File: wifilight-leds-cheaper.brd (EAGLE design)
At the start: 50.8 x 50.8 mm, 46 parts, among them Q1 BUK98180-100A, Q2 BUK98180-100A, Q3 BUK98180-100A, Q4 BUK98180-100A, U2 PCA9685

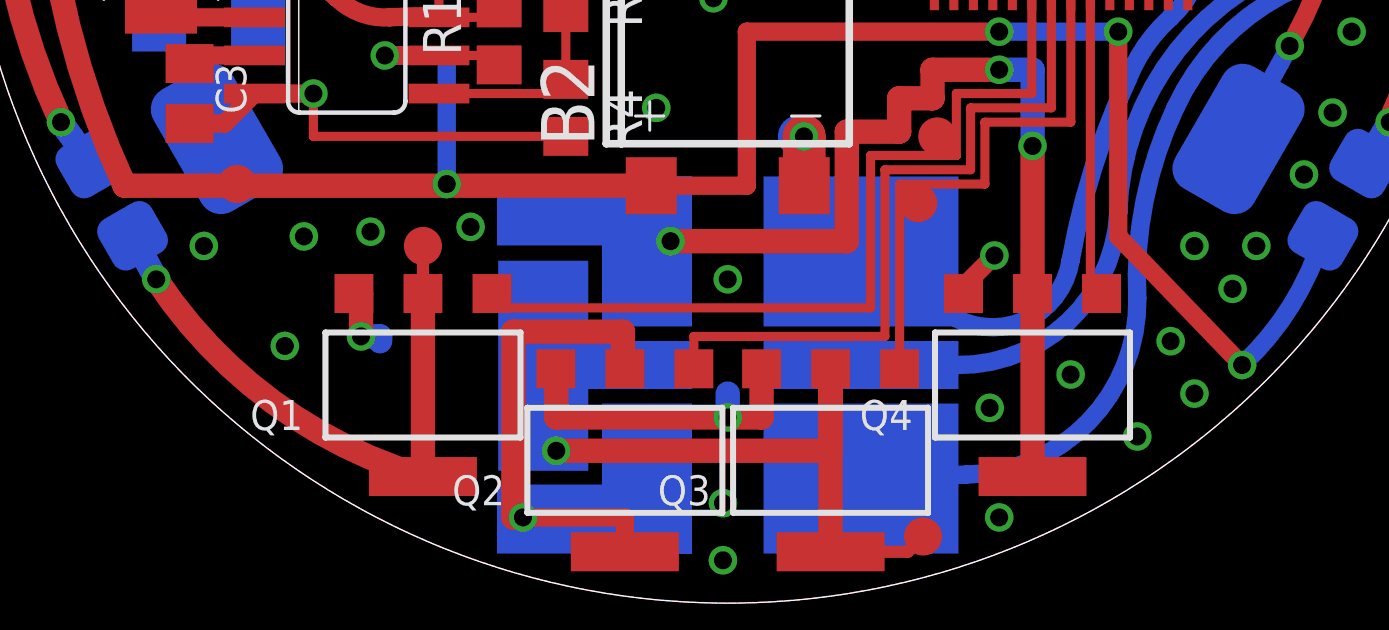
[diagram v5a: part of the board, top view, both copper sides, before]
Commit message: Add ground probe tag, drill locating hole in board.
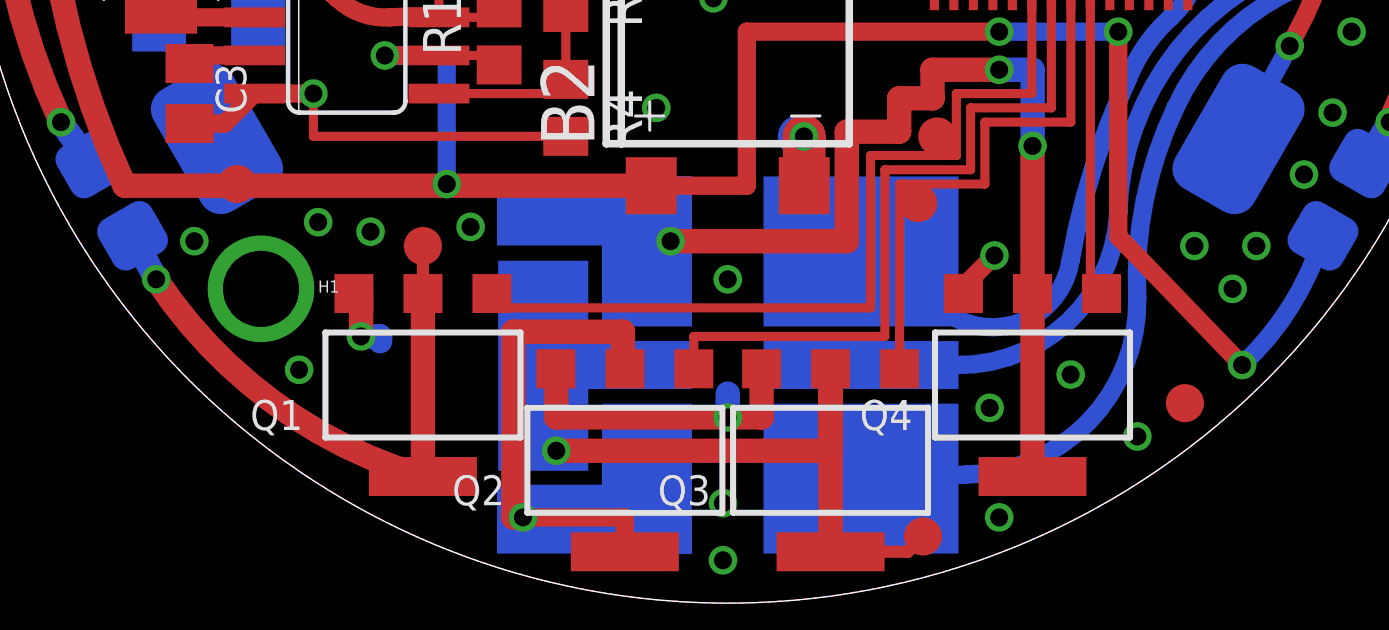
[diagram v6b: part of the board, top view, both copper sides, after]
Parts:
- added H1: SEW_HOLE, LilyPad-Wearables:SIMPLE_HOLE
- added TPGND: TEST-POINT3X5, SparkFun-Passives:PAD.03X.05
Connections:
- net GND: now also H1.P$1, TPGND.P$1
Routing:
- net GND: vias 75 -> 73
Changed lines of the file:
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@@
 <element name="P_WHITE" library="SparkFun-Passives" package="PAD.03X.05" value="TEST-POINT3X5" x="15.24" y="11.90625"/>
 <element name="P_RED" library="SparkFun-Passives" package="PAD.03X.05" value="TEST-POINT3X5" x="31.90875" y="2.2225"/>
+<element name="H1" library="LilyPad-Wearables" package="SIMPLE_HOLE" value="SEW_HOLE" x="9.8425" y="10.4775"/>
+<element name="TPGND" library="SparkFun-Passives" package="PAD.03X.05" value="TEST-POINT3X5" x="40.64" y="6.6675"/>
 </elements>
 <signals>
@@
 <via x="25.4" y="47.625" extent="1-16" drill="0.6"/>
 <via x="18.415" y="32.54375" extent="1-16" drill="0.6"/>
-<via x="7.9375" y="11.90625" extent="1-16" drill="0.6"/>
-<via x="11.27125" y="12.22375" extent="1-16" drill="0.6"/>
-<via x="10.63625" y="8.5725" extent="1-16" drill="0.6"/>
+<via x="7.62" y="12.065" extent="1-16" drill="0.6"/>
+<via x="11.7475" y="12.7" extent="1-16" drill="0.6"/>
+<via x="11.1125" y="7.77875" extent="1-16" drill="0.6"/>
 <via x="13.49375" y="12.3825" extent="1-16" drill="0.6"/>
 <via x="16.8275" y="12.54125" extent="1-16" drill="0.6"/>
@@
 <via x="34.44875" y="2.8575" extent="1-16" drill="0.6"/>
 <via x="39.0525" y="5.55625" extent="1-16" drill="0.6"/>
-<via x="40.9575" y="6.985" extent="1-16" drill="0.6"/>
-<via x="40.16375" y="8.73125" extent="1-16" drill="0.6"/>
 <via x="20.0025" y="26.19375" extent="1-16" drill="0.6"/>
 <via x="25.7175" y="26.82875" extent="1-16" drill="0.6"/>
@@
 <via x="24.92375" y="20.16125" extent="1-16" drill="0.6"/>
 <via x="23.01875" y="16.51" extent="1-16" drill="0.6"/>
+<contactref element="TPGND" pad="P$1"/>
+<contactref element="H1" pad="P$1"/>
 </signal>
 <signal name="SCL">

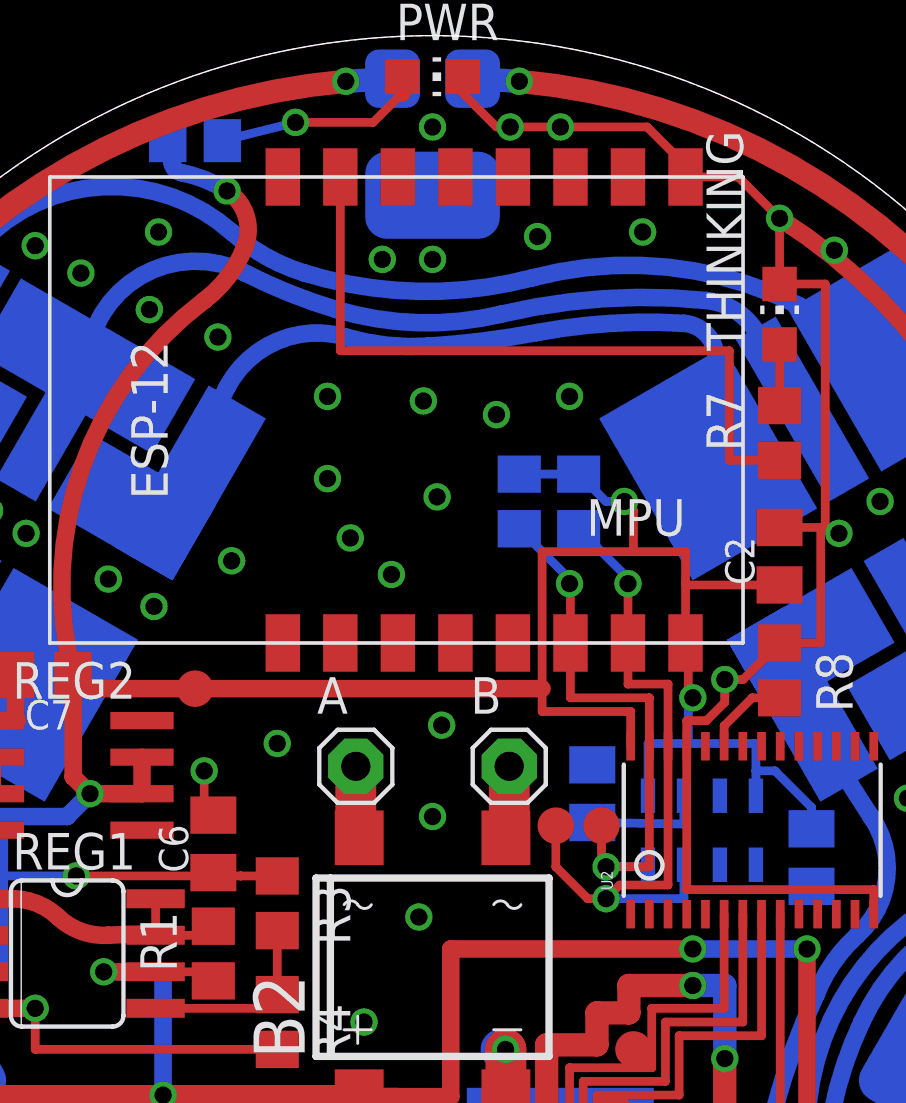
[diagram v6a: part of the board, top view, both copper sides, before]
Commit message: add SCL & SDA pins pogopins for programming
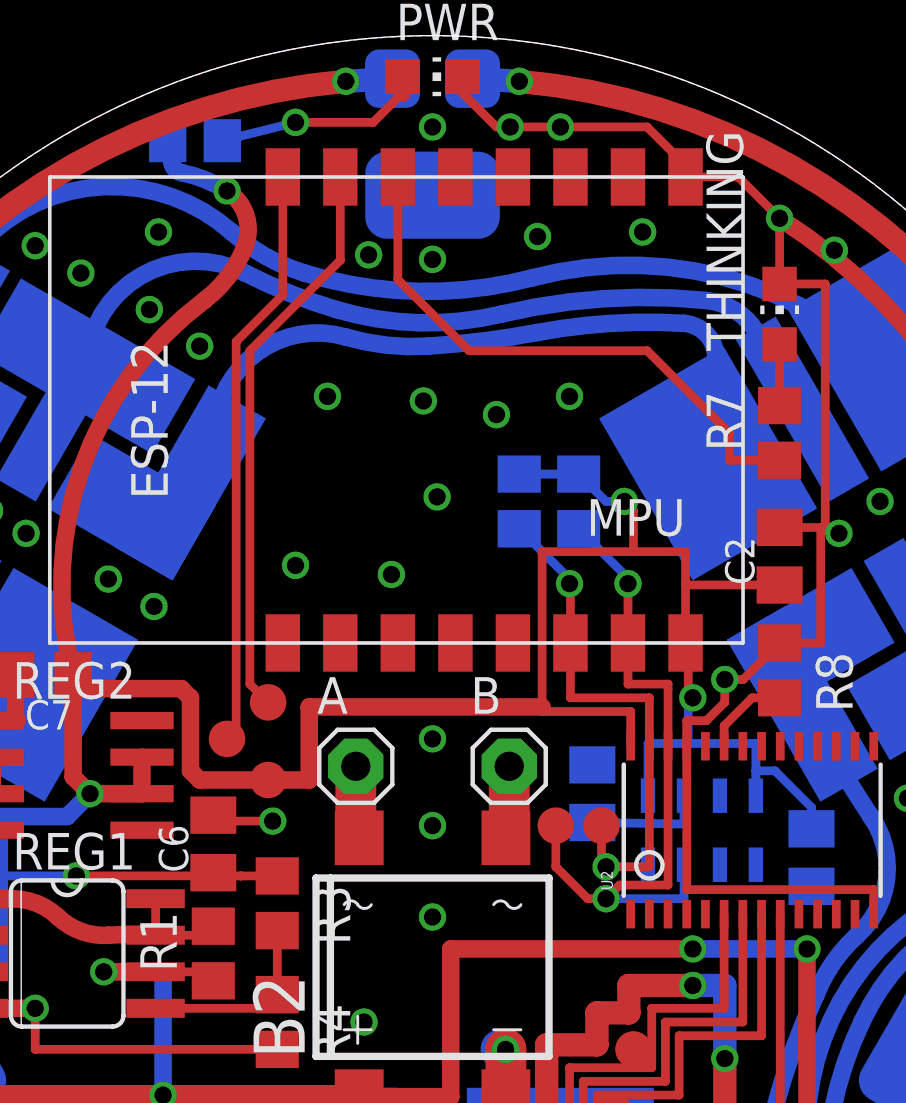
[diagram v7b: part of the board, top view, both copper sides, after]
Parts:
- added TPRX, TPTX: TEST-POINT3X5, SparkFun-Passives:PAD.03X.05
- moved TP3.3V 4.07 mm to (19.7, 24.9)
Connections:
- removed net N$29: MPU.9
- removed net N$32: MPU.6
- new net RXD: MPU.7, TPRX.P$1
- new net TXD: MPU.8, TPTX.P$1
- net RESET: now also MPU.9; no longer MPU.8
- net THINKING: now also MPU.6; no longer MPU.7
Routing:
- net TXD: track 0.00 -> 20.3 mm
- net RXD: track 0.00 -> 19.8 mm
- net 3.3V: track 96.0 -> 101.4 mm
- net THINKING: track 25.1 -> 20.0 mm
- net GND: track 128.2 -> 129.1 mm, vias 73 -> 70
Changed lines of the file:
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@@
 <element name="TP12V" library="SparkFun-Passives" package="PAD.03X.05" value="TEST-POINT3X5" x="9.04875" y="13.97"/>
 <element name="TP5V" library="SparkFun-Passives" package="PAD.03X.05" value="TEST-POINT3X5" x="4.7625" y="29.5275"/>
-<element name="TP3.3V" library="SparkFun-Passives" package="PAD.03X.05" value="TEST-POINT3X5" x="17.145" y="28.09875"/>
+<element name="TP3.3V" library="SparkFun-Passives" package="PAD.03X.05" value="TEST-POINT3X5" x="19.685" y="24.92375"/>
 <element name="SCL" library="SparkFun-Passives" package="PAD.03X.05" value="TEST-POINT3X5" x="29.68625" y="23.33625"/>
 <element name="SDA" library="SparkFun-Passives" package="PAD.03X.05" value="TEST-POINT3X5" x="31.27375" y="23.33625"/>
@@
 <element name="H1" library="LilyPad-Wearables" package="SIMPLE_HOLE" value="SEW_HOLE" x="9.8425" y="10.4775"/>
 <element name="TPGND" library="SparkFun-Passives" package="PAD.03X.05" value="TEST-POINT3X5" x="40.64" y="6.6675"/>
+<element name="TPTX" library="SparkFun-Passives" package="PAD.03X.05" value="TEST-POINT3X5" x="18.25625" y="26.3525"/>
+<element name="TPRX" library="SparkFun-Passives" package="PAD.03X.05" value="TEST-POINT3X5" x="19.685" y="27.6225"/>
 </elements>
 <signals>
@@
 <via x="6.35" y="26.51125" extent="1-16" drill="0.6"/>
 <wire x1="17.78" y1="23.70125" x2="17.4625" y2="23.70125" width="0.3048" layer="1"/>
-<wire x1="17.4625" y1="23.70125" x2="17.4625" y2="25.24125" width="0.3048" layer="1"/>
-<via x="17.4625" y="25.24125" extent="1-16" drill="0.6"/>
+<wire x1="17.4625" y1="23.70125" x2="17.78" y2="23.495" width="0.3048" layer="1"/>
+<wire x1="17.78" y1="23.495" x2="19.84375" y2="23.495" width="0.3048" layer="1"/>
+<via x="19.84375" y="23.495" extent="1-16" drill="0.6"/>
 <wire x1="38.89375" y1="33.655" x2="38.89375" y2="29.68625" width="0.3048" layer="1"/>
 <wire x1="38.89375" y1="29.68625" x2="37.465" y2="29.68625" width="0.3048" layer="1"/>
@@
 <via x="28.09875" y="47.625" extent="1-16" drill="0.6"/>
 <via x="29.845" y="47.625" extent="1-16" drill="0.6"/>
-<via x="17.93875" y="40.3225" extent="1-16" drill="0.6"/>
+<via x="17.30375" y="40.005" extent="1-16" drill="0.6"/>
 <via x="21.74875" y="38.25875" extent="1-16" drill="0.6"/>
-<via x="21.74875" y="35.40125" extent="1-16" drill="0.6"/>
-<via x="22.5425" y="33.3375" extent="1-16" drill="0.6"/>
 <via x="23.97125" y="32.0675" extent="1-16" drill="0.6"/>
 <via x="25.55875" y="34.76625" extent="1-16" drill="0.6"/>
@@
 <via x="30.1625" y="38.25875" extent="1-16" drill="0.6"/>
 <via x="25.4" y="47.625" extent="1-16" drill="0.6"/>
-<via x="18.415" y="32.54375" extent="1-16" drill="0.6"/>
+<via x="20.6375" y="32.385" extent="1-16" drill="0.6"/>
 <via x="7.62" y="12.065" extent="1-16" drill="0.6"/>
 <via x="11.7475" y="12.7" extent="1-16" drill="0.6"/>
@@
 <via x="15.875" y="43.97375" extent="1-16" drill="0.6"/>
 <via x="39.37" y="43.33875" extent="1-16" drill="0.6"/>
-<via x="23.65375" y="43.02125" extent="1-16" drill="0.6"/>
+<via x="23.1775" y="43.18" extent="1-16" drill="0.6"/>
 <via x="25.4" y="43.02125" extent="1-16" drill="0.6"/>
 <via x="29.05125" y="43.815" extent="1-16" drill="0.6"/>
@@
 <via x="34.44875" y="2.8575" extent="1-16" drill="0.6"/>
 <via x="39.0525" y="5.55625" extent="1-16" drill="0.6"/>
-<via x="20.0025" y="26.19375" extent="1-16" drill="0.6"/>
-<via x="25.7175" y="26.82875" extent="1-16" drill="0.6"/>
-<via x="25.4" y="23.65375" extent="1-16" drill="0.6"/>
-<via x="24.92375" y="20.16125" extent="1-16" drill="0.6"/>
+<via x="25.4" y="26.3525" extent="1-16" drill="0.6"/>
+<via x="25.4" y="23.33625" extent="1-16" drill="0.6"/>
+<via x="25.4" y="20.16125" extent="1-16" drill="0.6"/>
 <via x="23.01875" y="16.51" extent="1-16" drill="0.6"/>
 <contactref element="TPGND" pad="P$1"/>
@@
 <wire x1="34.195" y1="31.75" x2="34.195" y2="32.86125" width="0.3048" layer="1"/>
 <wire x1="34.195" y1="32.86125" x2="32.385" y2="32.86125" width="0.3048" layer="1"/>
-<wire x1="29.21" y1="32.86125" x2="29.21" y2="28.09875" width="0.3048" layer="1"/>
-<wire x1="29.21" y1="28.09875" x2="29.21" y2="27.305" width="0.3048" layer="1"/>
+<wire x1="29.21" y1="32.86125" x2="29.21" y2="27.46375" width="0.3048" layer="1"/>
+<wire x1="29.21" y1="27.46375" x2="29.21" y2="27.305" width="0.3048" layer="1"/>
 <wire x1="29.21" y1="27.305" x2="32.2875" y2="27.305" width="0.3048" layer="1"/>
 <wire x1="32.2875" y1="26.0953" x2="32.2875" y2="27.305" width="0.3048" layer="1"/>
@@
 <wire x1="32.0675" y1="34.6075" x2="31.43" y2="34.6075" width="0.3048" layer="16"/>
 <wire x1="31.43" y1="34.6075" x2="30.48" y2="35.5575" width="0.3048" layer="16"/>
-<wire x1="29.21" y1="28.09875" x2="17.145" y2="28.09875" width="0.6096" layer="1"/>
-<wire x1="17.145" y1="28.09875" x2="16.66875" y2="28.09875" width="0.6096" layer="1"/>
+<wire x1="29.21" y1="27.46375" x2="21.11375" y2="27.46375" width="0.6096" layer="1"/>
+<wire x1="21.11375" y1="27.46375" x2="21.11375" y2="24.92375" width="0.6096" layer="1"/>
+<wire x1="21.11375" y1="24.92375" x2="19.685" y2="24.92375" width="0.6096" layer="1"/>
+<wire x1="19.685" y1="24.92375" x2="17.30375" y2="24.92375" width="0.6096" layer="1"/>
+<wire x1="17.30375" y1="24.92375" x2="16.98625" y2="25.24125" width="0.6096" layer="1"/>
+<wire x1="16.98625" y1="25.24125" x2="16.98625" y2="27.78125" width="0.6096" layer="1"/>
+<wire x1="16.98625" y1="27.78125" x2="16.66875" y2="28.09875" width="0.6096" layer="1"/>
 <wire x1="16.66875" y1="28.09875" x2="12.90625" y2="28.09875" width="0.6096" layer="1"/>
 <wire x1="12.90625" y1="28.09875" x2="12.90625" y2="28.575" width="0.6096" layer="1"/>
@@
 <signal name="THINKING">
 <contactref element="R7" pad="1"/>
-<contactref element="MPU" pad="7"/>
-<wire x1="22.195" y1="45.88625" x2="22.195" y2="39.84625" width="0.3048" layer="1"/>
-<wire x1="22.195" y1="39.84625" x2="35.71875" y2="39.84625" width="0.3048" layer="1"/>
-<wire x1="35.71875" y1="39.84625" x2="35.71875" y2="36.03875" width="0.3048" layer="1"/>
+<wire x1="35.71875" y1="36.98875" x2="35.71875" y2="36.03875" width="0.3048" layer="1"/>
 <wire x1="35.71875" y1="36.03875" x2="37.465" y2="36.03875" width="0.3048" layer="1"/>
+<contactref element="MPU" pad="6"/>
+<wire x1="24.195" y1="45.88625" x2="24.195" y2="42.32125" width="0.3048" layer="1"/>
+<wire x1="24.195" y1="42.32125" x2="26.67" y2="39.84625" width="0.3048" layer="1"/>
+<wire x1="26.67" y1="39.84625" x2="32.86125" y2="39.84625" width="0.3048" layer="1"/>
+<wire x1="32.86125" y1="39.84625" x2="35.71875" y2="36.98875" width="0.3048" layer="1"/>
 </signal>
 <signal name="N$19">
@@
 <contactref element="MPU" pad="10"/>
 </signal>
-<signal name="N$29">
+<signal name="RESET">
 <contactref element="MPU" pad="9"/>
-</signal>
-<signal name="RESET">
-<contactref element="MPU" pad="8"/>
-</signal>
-<signal name="N$32">
-<contactref element="MPU" pad="6"/>
 </signal>
 <signal name="N$33">
@@
 <contactref element="MPU" pad="5"/>
 </signal>
+<signal name="TXD">
+<contactref element="MPU" pad="8"/>
+<contactref element="TPTX" pad="P$1"/>
+<wire x1="18.25625" y1="26.3525" x2="18.57375" y2="26.67" width="0.3048" layer="1"/>
+<wire x1="18.57375" y1="26.67" x2="18.57375" y2="40.16375" width="0.3048" layer="1"/>
+<wire x1="18.57375" y1="40.16375" x2="20.195" y2="41.785" width="0.3048" layer="1"/>
+<wire x1="20.195" y1="41.785" x2="20.195" y2="45.88625" width="0.3048" layer="1"/>
+</signal>
+<signal name="RXD">
+<contactref element="MPU" pad="7"/>
+<contactref element="TPRX" pad="P$1"/>
+<wire x1="19.685" y1="27.6225" x2="19.05" y2="28.2575" width="0.3048" layer="1"/>
+<wire x1="19.05" y1="28.2575" x2="19.05" y2="39.84625" width="0.3048" layer="1"/>
+<wire x1="19.05" y1="39.84625" x2="22.195" y2="42.99125" width="0.3048" layer="1"/>
+<wire x1="22.195" y1="42.99125" x2="22.195" y2="45.88625" width="0.3048" layer="1"/>
+</signal>
 </signals>
